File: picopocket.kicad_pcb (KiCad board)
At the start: 4 copper layers, 65.6 x 41.4 mm, 88 parts, among them IC1 AR1021, J1 Conn_02x40_Odd_Even, J2 Touchscreen, J3 Audio, Q1 BSS138, Q2 BSS138, U10 74LVC1G08, U11 74LVC1G34, U12 74LVC1G34, U13 74LVC32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

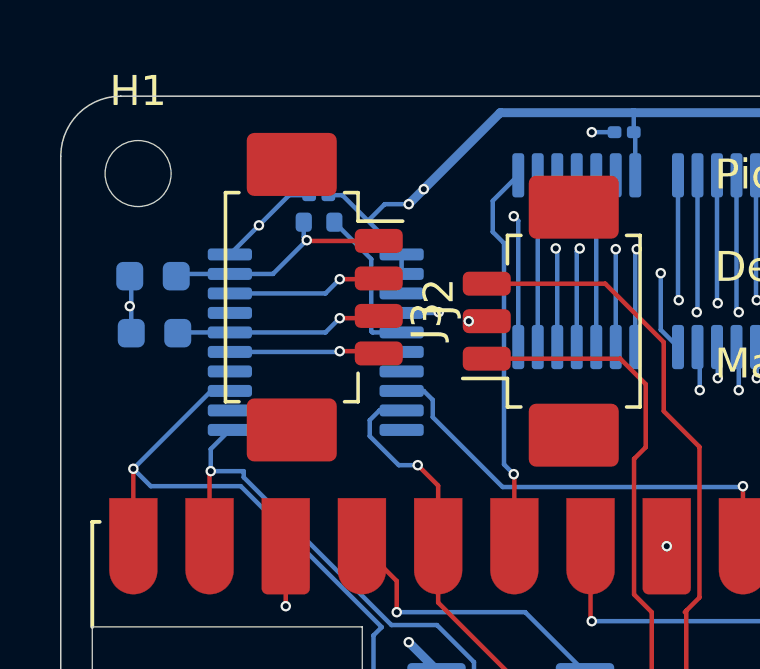
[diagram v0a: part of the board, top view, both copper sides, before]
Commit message: Fix AR1021 footprint
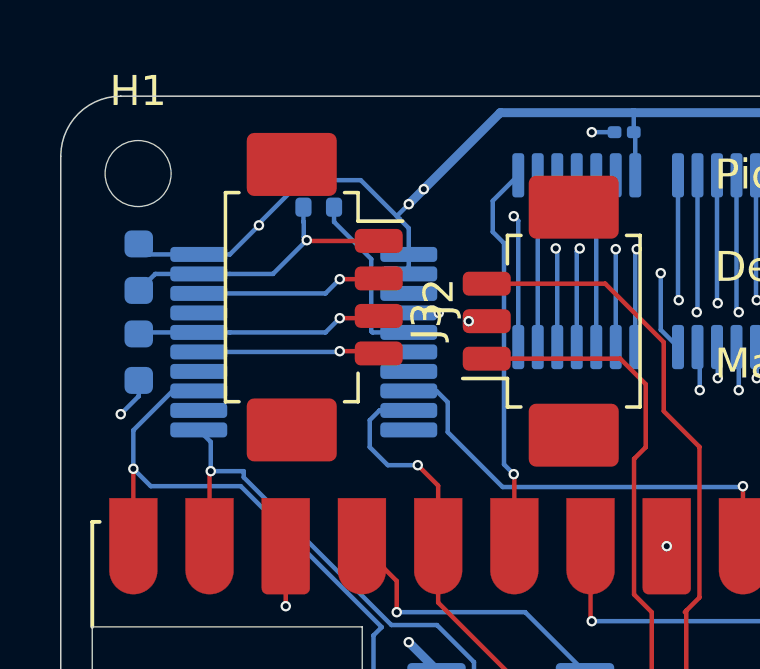
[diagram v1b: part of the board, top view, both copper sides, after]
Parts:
- IC1: footprint Package_SO:TSSOP-20_4.4x6.5mm_P0.65mm -> Package_SO:SSOP-20_5.3x7.2mm_P0.65mm
- moved C2 0.96 mm to (139.6, 94.2), turned to -90 degrees
- moved C1 0.56 mm to (139.6, 91.2), turned to 90 degrees
- moved R5 0.50 mm to (145.6, 89.2)
- moved C23 0.50 mm to (145.6, 88.3)
- moved IC1 0.40 mm to (145.1, 93.7)
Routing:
- net GND: track 110.8 -> 113.7 mm
- net Net-(IC1-X-): track 7.90 -> 10.6 mm
- net Net-(IC1-Y-): track 6.94 -> 8.96 mm
- net Net-(IC1-Y+): track 5.00 -> 6.04 mm
- net Net-(IC1-X+): track 5.17 -> 6.21 mm
- net Net-(IC1-WAKE): track 5.17 -> 5.68 mm

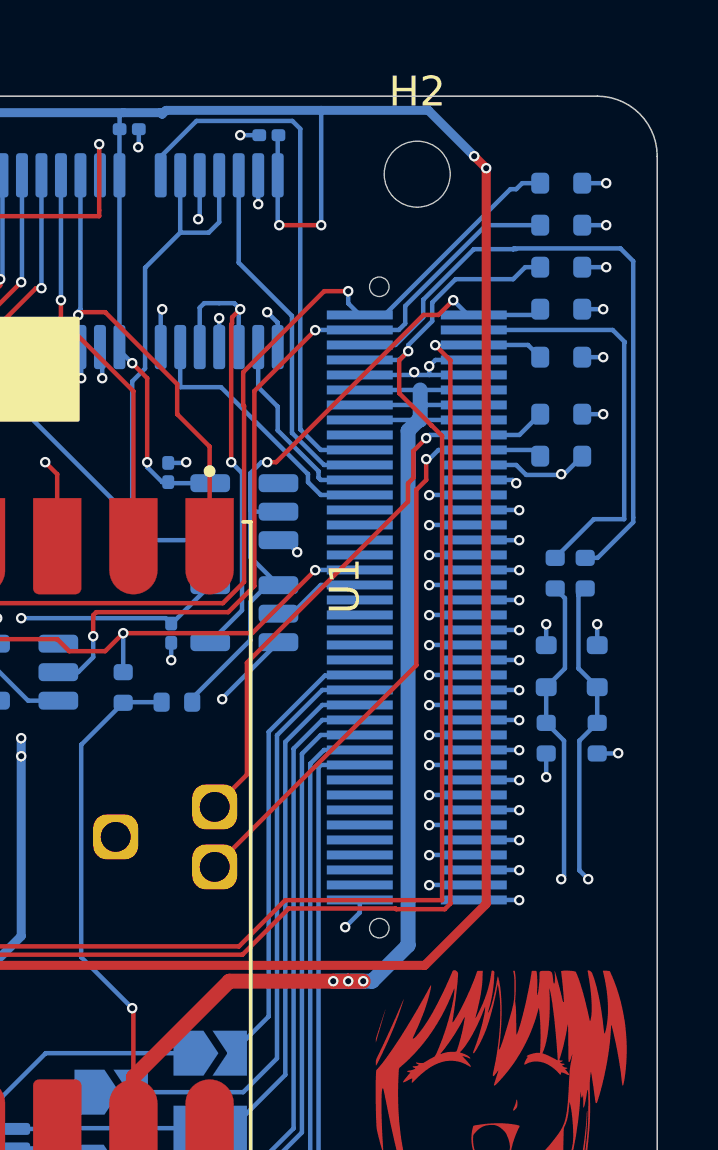
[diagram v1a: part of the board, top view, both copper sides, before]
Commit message: Fix divets in connector
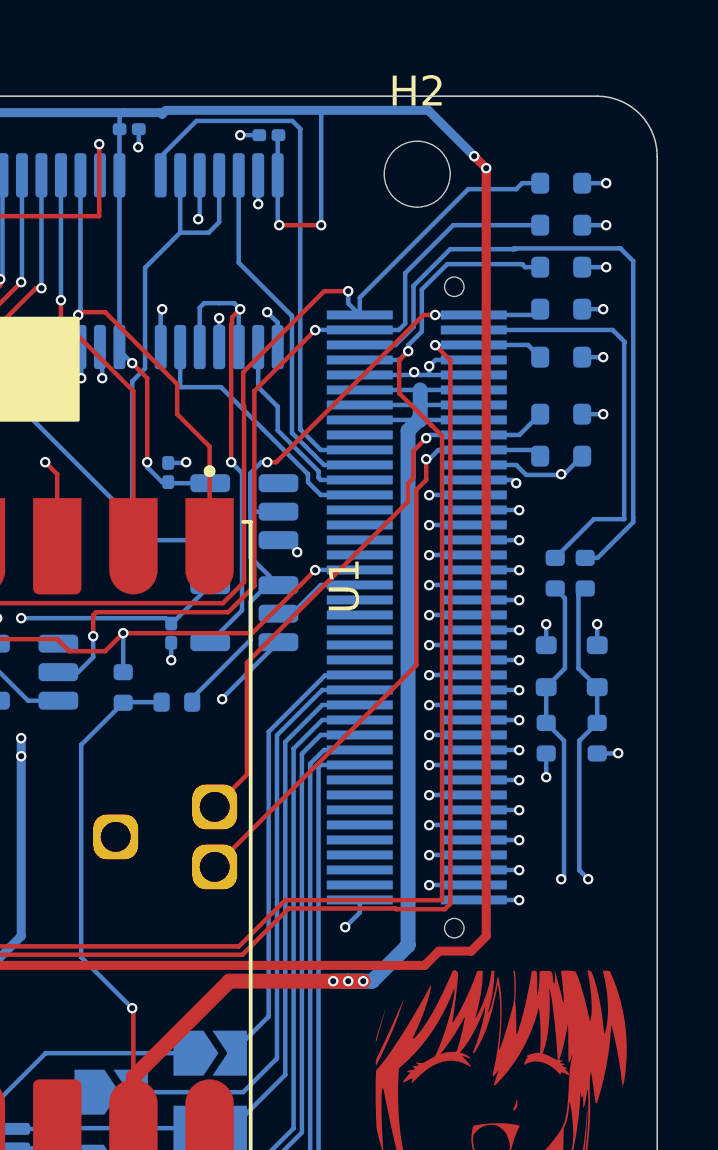
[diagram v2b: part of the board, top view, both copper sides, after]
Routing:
- net GIO3: track 27.2 -> 27.8 mm
- net +3.3V: track 269.9 -> 270.5 mm
- net GIO7: track 66.3 -> 66.8 mm
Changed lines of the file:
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@@
 			)
 		)
-		(property ki_fp_filters "Connector*:*_2x??_*")
-		(sheetname "Root")
-		(sheetfile "picopocket.kicad_sch")
 		(attr smd)
 		(fp_rect
@@
 		)
 		(pad "" np_thru_hole circle
-			(at 3.25 -21.94 180)
+			(at 0.75 -21.94 180)
 			(size 0.65 0.65)
 			(drill 0.65)
@@
 		)
 		(pad "" np_thru_hole circle
-			(at 3.25 -0.56 180)
+			(at 0.75 -0.56 180)
 			(size 0.65 0.65)
 			(drill 0.65)
@@
 	)
 	(segment
-		(start 192.686308 93.292901)
-		(end 193.986308 93.292901)
+		(start 194.2 93.079209)
+		(end 194.2 91.4)
+		(width 0.15)
+		(layer "B.Cu")
+		(net 13)
+	)
+	(segment
+		(start 194.2 91.4)
+		(end 195.8 89.8)
 		(width 0.15)
 		(layer "B.Cu")
@@
 	)
 	(segment
-		(start 193.986308 93.292901)
-		(end 194.2 93.079209)
+		(start 195.8 89.8)
+		(end 198.7 89.8)
 		(width 0.15)
 		(layer "B.Cu")
@@
 	)
 	(segment
-		(start 196.895735 89.8)
-		(end 198.7 89.8)
+		(start 193.986308 93.292901)
+		(end 194.2 93.079209)
 		(width 0.15)
 		(layer "B.Cu")
@@
 	)
 	(segment
-		(start 194.2 93.079209)
-		(end 194.2 92.495735)
+		(start 192.686308 93.292901)
+		(end 193.986308 93.292901)
 		(width 0.15)
 		(layer "B.Cu")
@@
 	)
 	(segment
-		(start 194.2 92.495735)
-		(end 196.895735 89.8)
-		(width 0.15)
-		(layer "B.Cu")
-		(net 13)
-	)
-	(segment
 		(start 189.1 123.7)
 		(end 185.05 123.7)
@@
 	)
 	(segment
-		(start 201.8 91)
-		(end 201.8 99.544804)
+		(start 194.477 93.193946)
+		(end 194.477 91.823)
 		(width 0.15)
 		(layer "B.Cu")
@@
 	)
 	(segment
-		(start 196.487472 90.6)
-		(end 197.8 90.6)
+		(start 201.8 91)
+		(end 201.8 99.544804)
 		(width 0.15)
 		(layer "B.Cu")
@@
 	)
 	(segment
-		(start 201.8 99.7)
-		(end 200.61 100.89)
+		(start 193.878046 93.792901)
+		(end 194.477 93.193946)
 		(width 0.15)
 		(layer "B.Cu")
@@
 	)
 	(segment
-		(start 194.8 92.287472)
-		(end 196.487472 90.6)
+		(start 201.8 99.7)
+		(end 200.61 100.89)
 		(width 0.15)
 		(layer "B.Cu")
@@
 	)
 	(segment
-		(start 201.375 90.575)
-		(end 201.8 91)
+		(start 195.7 90.6)
+		(end 197.8 90.6)
 		(width 0.15)
 		(layer "B.Cu")
@@
 	)
 	(segment
-		(start 201.8 99.544804)
-		(end 201.8 99.7)
+		(start 201.375 90.575)
+		(end 201.8 91)
 		(width 0.15)
 		(layer "B.Cu")
@@
 	)
 	(segment
-		(start 193.878046 93.792901)
-		(end 194.8 92.870947)
+		(start 201.8 99.544804)
+		(end 201.8 99.7)
 		(width 0.15)
 		(layer "B.Cu")
@@
 	)
 	(segment
-		(start 194.8 92.870947)
-		(end 194.8 92.287472)
+		(start 194.477 91.823)
+		(end 195.7 90.6)
 		(width 0.15)
 		(layer "B.Cu")
@@
 	)
 	(segment
-		(start 194.3 94)
-		(end 194.3 93.8)
+		(start 198.1 91.1)
+		(end 198.2 91.2)
 		(width 0.15)
 		(layer "B.Cu")
@@
 	)
 	(segment
-		(start 195.879209 91.6)
-		(end 197.8 91.6)
+		(start 194.3 94)
+		(end 194.3 93.8)
 		(width 0.15)
 		(layer "B.Cu")
@@
 	)
 	(segment
-		(start 197.8 91.6)
-		(end 198.2 91.2)
+		(start 194.754 93.346)
+		(end 194.754 91.946)
 		(width 0.15)
 		(layer "B.Cu")
@@
 	)
 	(segment
-		(start 198.2 91.2)
-		(end 198.7 91.2)
+		(start 194.754 91.946)
+		(end 195.6 91.1)
 		(width 0.15)
 		(layer "B.Cu")
@@
 	)
 	(segment
-		(start 194.3 94)
-		(end 194.007099 94.292901)
+		(start 194.3 93.8)
+		(end 194.754 93.346)
 		(width 0.15)
 		(layer "B.Cu")
@@
 	)
 	(segment
-		(start 195.1 92.379209)
-		(end 195.879209 91.6)
+		(start 194.3 94)
+		(end 194.007099 94.292901)
 		(width 0.15)
 		(layer "B.Cu")
@@
 	)
 	(segment
-		(start 195.1 93)
-		(end 195.1 92.379209)
+		(start 198.2 91.2)
+		(end 198.7 91.2)
 		(width 0.15)
 		(layer "B.Cu")
@@
 	)
 	(segment
-		(start 194.3 93.8)
-		(end 195.1 93)
+		(start 195.6 91.1)
+		(end 198.1 91.1)
 		(width 0.15)
 		(layer "B.Cu")
@@
 	)
 	(segment
+		(start 180.427 114.473)
+		(end 177.6 117.3)
+		(width 0.3)
+		(layer "F.Cu")
+		(net 69)
+	)
+	(segment
 		(start 177.6 117.9)
 		(end 177.6 119.8)
@@
 	)
 	(segment
-		(start 196.9 112.424344)
-		(end 194.851344 114.473)
-		(width 0.3)
-		(layer "F.Cu")
-		(net 69)
-	)
-	(segment
 		(start 185.1 94.4)
 		(end 185.6 94.9)
@@
 	)
 	(segment
-		(start 194.851344 114.473)
-		(end 180.427 114.473)
+		(start 196.9 87.9)
+		(end 196.9 113.5)
 		(width 0.3)
 		(layer "F.Cu")
@@
 	)
 	(segment
+		(start 196.9 113.5)
+		(end 196.4 114)
+		(width 0.3)
+		(layer "F.Cu")
+		(net 69)
+	)
+	(segment
 		(start 196.5 87.5)
 		(end 196.9 87.9)
@@
 	)
 	(segment
-		(start 196.9 87.9)
-		(end 196.9 112.424344)
+		(start 194.851344 114.473)
+		(end 180.427 114.473)
 		(width 0.3)
 		(layer "F.Cu")
@@
 	)
 	(segment
-		(start 180.427 114.473)
-		(end 177.6 117.3)
+		(start 196.4 114)
+		(end 195.324344 114)
+		(width 0.3)
+		(layer "F.Cu")
+		(net 69)
+	)
+	(segment
+		(start 195.324344 114)
+		(end 194.851344 114.473)
 		(width 0.3)
 		(layer "F.Cu")
@@
 	)
 	(segment
-		(start 189.9 97.7)
-		(end 189.6 97.7)
+		(start 195.2 92.792901)
+		(end 194.807099 92.792901)
 		(width 0.15)
 		(layer "F.Cu")
@@
 	)
 	(segment
-		(start 195.307099 92.792901)
-		(end 194.807099 92.792901)
-		(width 0.15)
-		(layer "F.Cu")
-		(net 80)
-	)
-	(segment
-		(start 195.8 92.3)
-		(end 195.307099 92.792901)
+		(start 189.9 97.7)
+		(end 189.6 97.7)
 		(width 0.15)
 		(layer "F.Cu")
@@
 	)
 	(via
-		(at 195.8 92.3)
+		(at 195.2 92.792901)
 		(size 0.35)
 		(drill 0.2)
@@
 	)
 	(segment
+		(start 195.2 92.792901)
+		(end 196.292901 92.792901)
+		(width 0.15)
+		(layer "B.Cu")
+		(net 80)
+	)
+	(segment
 		(start 189.0375 100.8625)
 		(end 189.975 101.8)
@@
 	)
 	(segment
-		(start 195.8 92.3)
-		(end 196.292901 92.792901)
-		(width 0.15)
-		(layer "B.Cu")
-		(net 80)
-	)
-	(segment
 		(start 189.0375 102.3625)
 		(end 189.6 101.8)
@@
 	)
 	(segment
-		(start 193.511096 92.792901)
-		(end 197.703997 88.6)
+		(start 192.686308 92.792901)
+		(end 192.686308 92.213692)
 		(width 0.15)
 		(layer "B.Cu")
@@
 	)
 	(segment
-		(start 197.9 88.6)
-		(end 198.1 88.4)
+		(start 167.55 105.85)
+		(end 167.6 105.8)
 		(width 0.15)
 		(layer "B.Cu")
@@
 	)
 	(segment
-		(start 167.55 105.85)
-		(end 167.6 105.8)
+		(start 196.3 88.6)
+		(end 197.9 88.6)
 		(width 0.15)
 		(layer "B.Cu")
@@
 	)
 	(segment
-		(start 192.3 92.406593)
-		(end 192.686308 92.792901)
+		(start 192.686308 92.213692)
+		(end 196.3 88.6)
 		(width 0.15)
 		(layer "B.Cu")
@@
 	)
 	(segment
-		(start 198.1 88.4)
-		(end 198.7 88.4)
+		(start 192.3 92.406593)
+		(end 192.686308 92.792901)
 		(width 0.15)
 		(layer "B.Cu")
@@
 	)
 	(segment
-		(start 197.703997 88.6)
-		(end 197.9 88.6)
+		(start 198.1 88.4)
+		(end 198.7 88.4)
 		(width 0.15)
 		(layer "B.Cu")
@@
 	)
 	(segment
-		(start 192.686308 92.792901)
-		(end 193.511096 92.792901)
+		(start 197.9 88.6)
+		(end 198.1 88.4)
 		(width 0.15)
 		(layer "B.Cu")

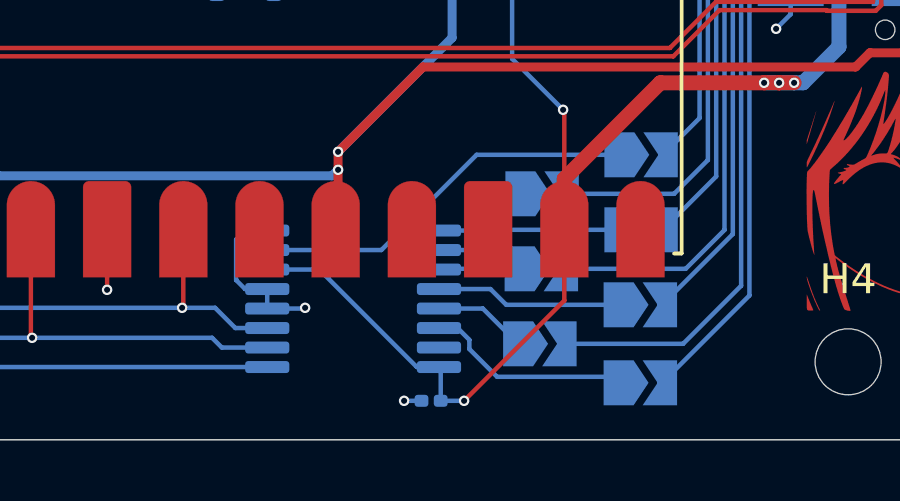
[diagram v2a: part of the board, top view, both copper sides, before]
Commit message: Change to 74HC238 (avalibility)
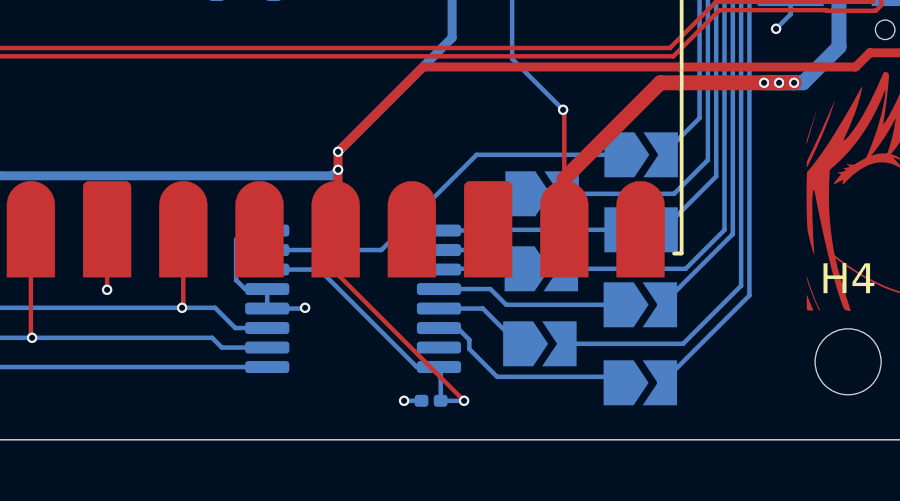
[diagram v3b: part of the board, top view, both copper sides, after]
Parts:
- U14: value 74HCT238 -> 74HC238
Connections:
- C28 pad 1: +5V -> +3.3V
- U14 pad 16: +5V -> +3.3V
- U14 pad 6: +5V -> +3.3V
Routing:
- net +3.3V: track 270.5 -> 287.0 mm, vias 15 -> 16
- net +5V: track 76.6 -> 60.5 mm, vias 5 -> 4
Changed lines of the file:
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@@
 			)
 		)
-		(property "Value" "74HCT238"
+		(property "Value" "74HC238"
 			(at 0 -3.45 360)
 			(layer "B.Fab")
@@
 			(layers "B.Cu" "B.Paste" "B.Mask")
 			(roundrect_rratio 0.25)
-			(net 9 "+5V")
+			(net 69 "+3.3V")
 			(pinfunction "G1")
 			(pintype "input")
@@
 			(layers "B.Cu" "B.Paste" "B.Mask")
 			(roundrect_rratio 0.25)
-			(net 9 "+5V")
+			(net 69 "+3.3V")
 			(pinfunction "VCC")
 			(pintype "power_in")
@@
 			)
 		)
+		(property ki_fp_filters "Connector*:*_2x??_*")
+		(sheetname "Root")
+		(sheetfile "picopocket.kicad_sch")
 		(attr smd)
 		(fp_rect
@@
 			(layers "B.Cu" "B.Mask")
 			(roundrect_rratio 0.25)
-			(net 9 "+5V")
+			(net 69 "+3.3V")
 			(pintype "passive")
 		)
@@
 	)
 	(segment
-		(start 185.14 119.88)
-		(end 185.14 122.26)
-		(width 0.15)
-		(layer "F.Cu")
-		(net 9)
-	)
-	(segment
 		(start 185.1 115.9)
 		(end 185.14 115.94)
@@
 	)
 	(segment
-		(start 185.14 122.26)
-		(end 181.8 125.6)
-		(width 0.15)
-		(layer "F.Cu")
-		(net 9)
-	)
-	(segment
 		(start 191.8 115)
 		(end 188.34 115)
@@
 	)
 	(via
-		(at 181.8 125.6)
-		(size 0.35)
-		(drill 0.2)
-		(layers "F.Cu" "B.Cu")
-		(net 9)
-	)
-	(via
 		(at 192.8 115)
 		(size 0.35)
@@
 	)
 	(segment
-		(start 181.02 124.5325)
-		(end 180.9625 124.475)
-		(width 0.15)
-		(layer "B.Cu")
-		(net 9)
-	)
-	(segment
 		(start 194.7 95.292901)
 		(end 194.7 95.792901)
@@
 	)
 	(segment
-		(start 181.02 125.6)
-		(end 181.02 124.5325)
-		(width 0.15)
-		(layer "B.Cu")
-		(net 9)
-	)
-	(segment
 		(start 183.4 114.2)
 		(end 185.1 115.9)
@@
 	)
 	(segment
-		(start 180.225001 124.475)
-		(end 176.975001 121.225)
-		(width 0.15)
-		(layer "B.Cu")
-		(net 9)
-	)
-	(segment
-		(start 180.9625 124.475)
-		(end 180.225001 124.475)
-		(width 0.15)
-		(layer "B.Cu")
-		(net 9)
-	)
-	(segment
 		(start 193.1 115)
 		(end 192.8 115)
@@
 	)
 	(segment
-		(start 181.8 125.6)
-		(end 181.02 125.6)
-		(width 0.15)
-		(layer "B.Cu")
-		(net 9)
-	)
-	(segment
 		(start 196.486308 95.292901)
 		(end 194.7 95.292901)
@@
 	)
 	(segment
-		(start 176.975001 121.225)
-		(end 175.2375 121.225)
-		(width 0.15)
-		(layer "B.Cu")
-		(net 9)
-	)
-	(segment
 		(start 194.7 95.792901)
 		(end 194.7 96.292901)
@@
 	)
 	(segment
+		(start 181.8 125.6)
+		(end 177.52 121.32)
+		(width 0.15)
+		(layer "F.Cu")
+		(net 69)
+	)
+	(segment
 		(start 185.6 94.9)
 		(end 185.6 97.7)
@@
 	)
 	(segment
+		(start 177.52 121.32)
+		(end 177.52 119.88)
+		(width 0.15)
+		(layer "F.Cu")
+		(net 69)
+	)
+	(segment
 		(start 194.851344 114.473)
 		(end 180.427 114.473)
@@
 	)
 	(via
+		(at 181.8 125.6)
+		(size 0.35)
+		(drill 0.2)
+		(layers "F.Cu" "B.Cu")
+		(net 69)
+	)
+	(via
 		(at 177.6 117.9)
 		(size 0.35)
@@
 	)
 	(segment
+		(start 181.02 124.5325)
+		(end 180.9625 124.475)
+		(width 0.15)
+		(layer "B.Cu")
+		(net 69)
+	)
+	(segment
 		(start 186.42 103.08)
 		(end 186.4 103.08)
@@
 	)
 	(segment
+		(start 181.02 125.6)
+		(end 181.02 124.5325)
+		(width 0.15)
+		(layer "B.Cu")
+		(net 69)
+	)
+	(segment
 		(start 163.48 86.7)
 		(end 163.48 86.13)
@@
 	)
 	(segment
+		(start 180.225001 124.475)
+		(end 176.975001 121.225)
+		(width 0.15)
+		(layer "B.Cu")
+		(net 69)
+	)
+	(segment
+		(start 180.9625 124.475)
+		(end 180.225001 124.475)
+		(width 0.15)
+		(layer "B.Cu")
+		(net 69)
+	)
+	(segment
 		(start 185.6 97.864999)
 		(end 186.100001 98.365)
@@
 	)
 	(segment
+		(start 181.8 125.6)
+		(end 181.02 125.6)
+		(width 0.15)
+		(layer "B.Cu")
+		(net 69)
+	)
+	(segment
 		(start 148.3 89.6)
 		(end 147 88.3)
@@
 		(layer "B.Cu")
 		(net 69)
+	)
+	(segment
+		(start 176.975001 121.225)
+		(end 175.2375 121.225)
+		(width 0.15)
+		(layer "B.Cu")
+		(net 69)
